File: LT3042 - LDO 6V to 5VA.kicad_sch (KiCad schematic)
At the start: 17 parts, among them IC2 TPS61086DRCR

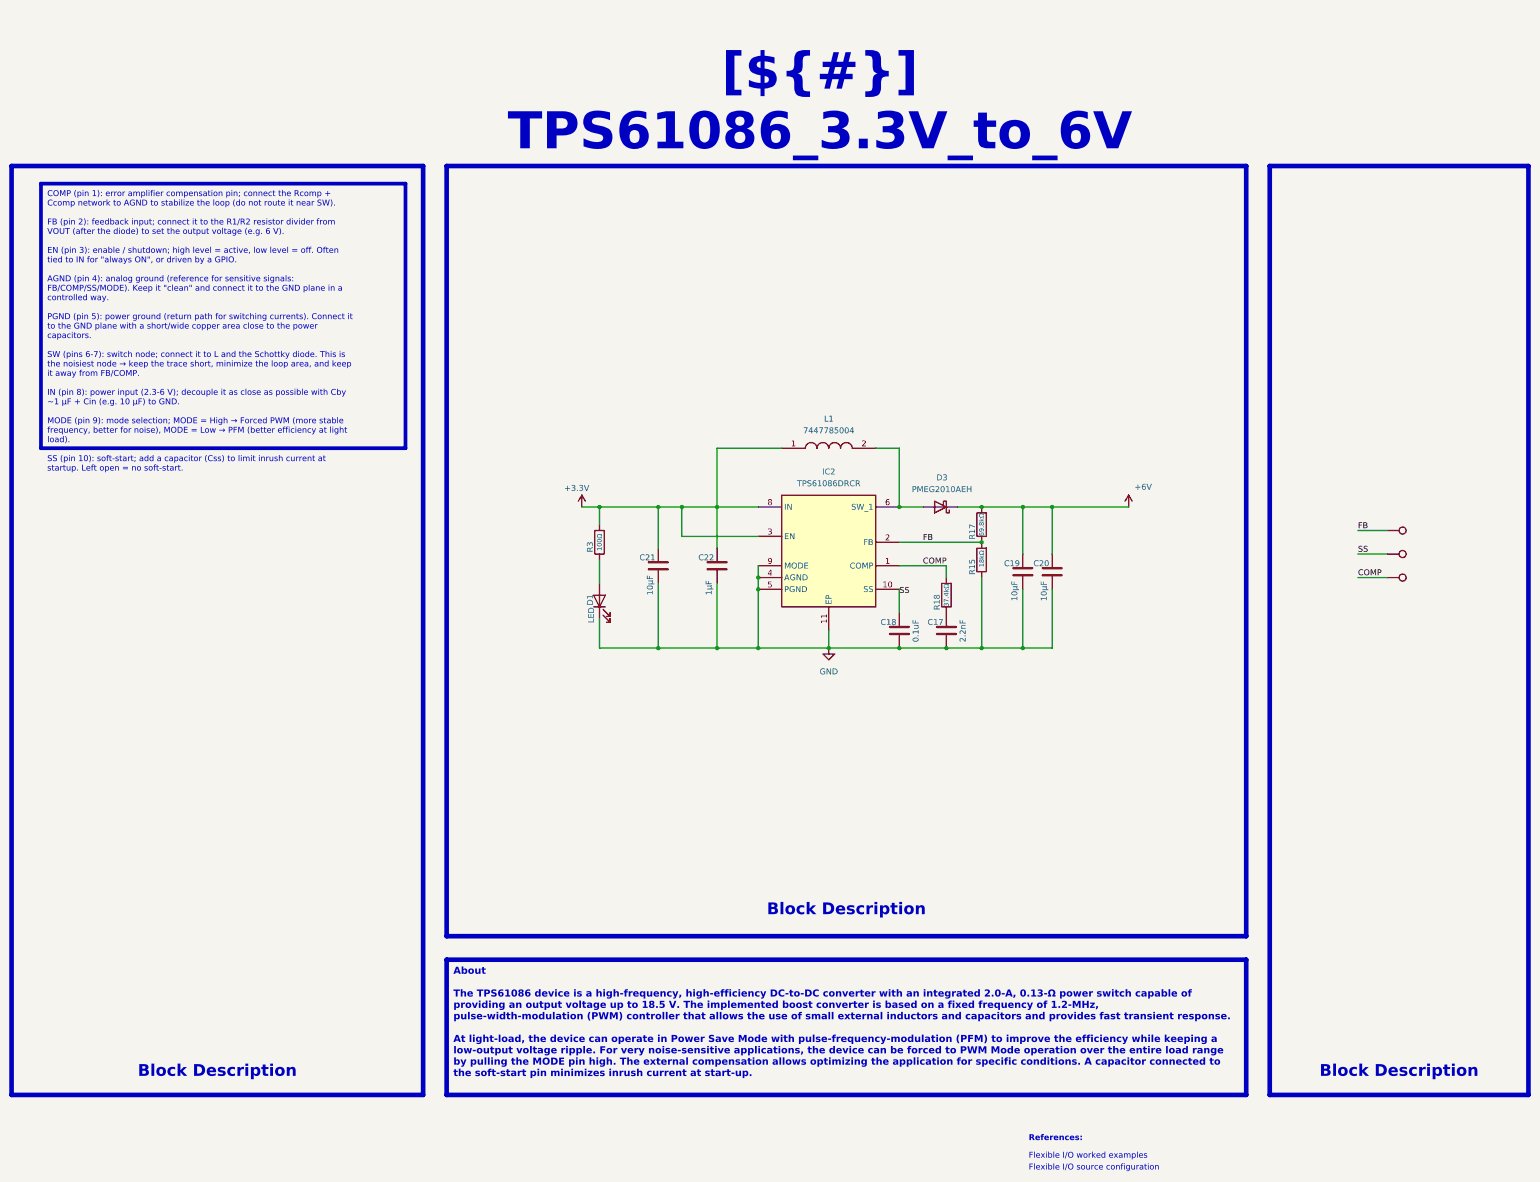
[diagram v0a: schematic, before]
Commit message: Clean up project for KDT template: rename, metadata, KiCad 10 CI
- Rename project Cellule_de_force_V2 -> OPEN_WEIGHT and sheets after their function
  (fix AD7910 -> AD7190 typo), update all sheet/project references in sch/pcb/pro
- Real title-block titles, sheet headers use ${TITLE}, restore KDT drawing sheets,
  remove template leftovers from PCB title block
- kibot_main.yaml: COMPANY = OPEN THRUST LAB, GIT_URL = foukouda/OPEN_WEIGHT
- CI: add KiCad 10 (KiBot v2_dk10), PRELIMINARY variant on dev
- README now generated from kibot_resources/templates/readme.txt; fill CHANGELOG
- Move mechanical CAD to Mechanical/, extend .gitignore, untrack 3Dx logs

Co-Authored-By: Claude Opus 5.5 <noreply@anthropic.com>
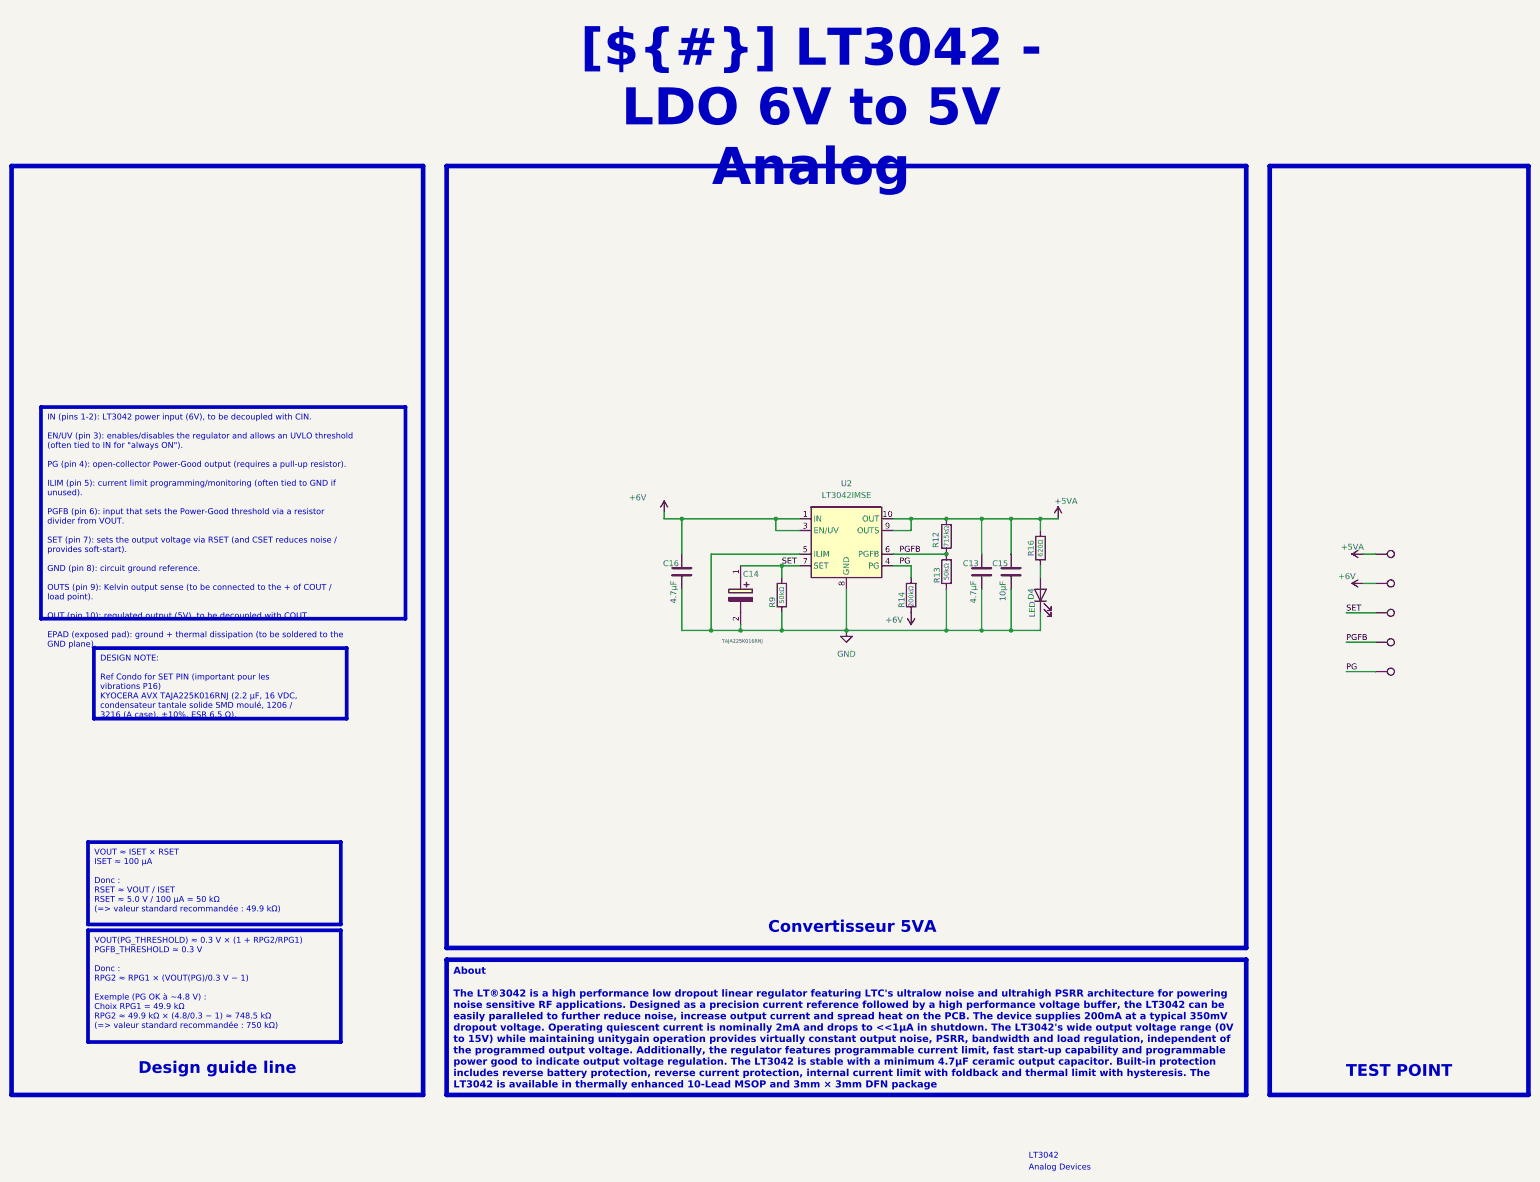
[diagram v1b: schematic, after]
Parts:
- removed C17: 2.2nF, Capacitor_SMD:C_0603_1608Metric, symbol Device:C
- removed C18: 0.1uF, Capacitor_SMD:C_0603_1608Metric, symbol Device:C
- removed C19, C20, C21: 10µF, Capacitor_SMD:C_0603_1608Metric, symbol Device:C
- removed C22: 1µF, Capacitor_SMD:C_0603_1608Metric, symbol Device:C
- removed D1: LED, LED_SMD:LED_0603_1608Metric, symbol Device:LED
- removed D3: PMEG2010AEH, Diode_SMD:D_SOD-123F, symbol Diode:PMEG2010AEH
- removed IC2: TPS61086DRCR, TPS61086DRCR:TPS16412DRCR, symbol TPS61086DRCR:TPS61086DRCR
- removed L1: 7447785004, 7447785004:7447785004, symbol 7447785004:7447785004
- removed R15: 18kΩ, Resistor_SMD:R_0603_1608Metric, symbol Device:R
- removed R17: 69.8kΩ, Resistor_SMD:R_0603_1608Metric, symbol Device:R
- removed R18: 37.4kΩ, Resistor_SMD:R_0603_1608Metric, symbol Device:R
- removed R3: 100Ω, Resistor_SMD:R_0603_1608Metric, symbol Device:R
- removed TP14, TP15, TP16: TestPoint, TestPoint:TestPoint_Pad_D1.5mm, symbol Connector:TestPoint
- added C13, C16: 4.7µF, Capacitor_SMD:C_0603_1608Metric, symbol Device:C
- added C14: TAJA225K016RNJ, CAPPM3216X180N, symbol TAJA225K016RNJ:TAJA225K016RNJ
- added C15: 10µF, Capacitor_SMD:C_0603_1608Metric, symbol Device:C
- added D4: LED, LED_SMD:LED_0603_1608Metric, symbol Device:LED
- added R12: 715kΩ, Resistor_SMD:R_0603_1608Metric, symbol Device:R
- added R13, R9: 50kΩ, Resistor_SMD:R_0603_1608Metric, symbol Device:R
- added R14: 200kΩ, Resistor_SMD:R_0603_1608Metric, symbol Device:R
- added R16: 620Ω, Resistor_SMD:R_0603_1608Metric, symbol Device:R
- added TP10, TP11, TP12, TP13, TP17: TestPoint, TestPoint:TestPoint_Pad_D1.5mm, symbol Connector:TestPoint
- added U2: LT3042IMSE, Package_SO:MSOP-10-1EP_3x3mm_P0.5mm_EP2.2x3.1mm_Mask1.83x1.89mm_ThermalVias, symbol Regulator_Linear:LT3042xMSE
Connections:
- net +6V: now also C16.1, R14.1, TP11.1, U2.1 (IN), U2.2 (IN), U2.3 (EN/UV)
- net GND: now also C13.2, C14.2 (-), C15.2, C16.2, D4.1 (K), R13.1, R9.1, U2.11 (GND), U2.5 (ILIM), U2.8 (GND)
- new net: D4.2 (A), R16.1
- new net +5VA: C13.1, C15.1, R12.2, R16.2, TP10.1, U2.10 (OUT), U2.9 (OUTS)
- new net PG: R14.2, TP17.1, U2.4 (PG)
- new net PGFB: R12.1, R13.2, TP13.1, U2.6 (PGFB)
- new net SET: C14.1 (+), R9.2, TP12.1, U2.7 (SET)
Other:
- note added: "Analog Devices"
- note added: "LT3042"
- note removed: "Flexible I/O source configuration"
- note removed: "Flexible I/O worked examples"
- note removed: "References:"
- title: Sheet Title B -> LT3042 - LDO 6V to 5V Analog

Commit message: Self-contained libraries, JLCPCB rules, ERC/DRC cleanup
- lib/: project symbol library (19 symbols), footprint library (17 footprints)
  and all 3D models (15), referenced through ${KIPRJMOD} + project lib tables.
  A fresh clone now opens with every symbol, footprint and 3D model.
- Remove duplicated / absolute 3D model paths (C:/Users/..., ${KICAD_FOOTPRINT})
- OPEN_WEIGHT.kicad_dru: JLCPCB 4-layer rules; stackup JLC04161H-7628; board minimums
- AD7190 footprint: drop per-pad 0.102 mm mask margin (mask bridges at 0.65 mm pitch)
- Exclude unplaced TP/FID symbols from board; PWR_FLAGs; decorative wires -> lines
- Local text variables in .kicad_pro; Revision History wired to [Unreleased]
- get_changelog.py: accept "## [Unreleased]" without date
ERC: 0 errors. DRC: 0 errors except 10 courtyard overlaps (placement), 0 parity issues.

Co-Authored-By: Claude Opus 5.5 <noreply@anthropic.com>
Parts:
- C13, C15, C16: footprint Capacitor_SMD:C_0603_1608Metric -> OPEN_WEIGHT:C_0603_1608Metric; symbol Device:C -> OPEN_WEIGHT:C
- C14: footprint CAPPM3216X180N -> OPEN_WEIGHT:CAPPM3216X180N; symbol TAJA225K016RNJ:TAJA225K016RNJ -> OPEN_WEIGHT:TAJA225K016RNJ
- D4: footprint LED_SMD:LED_0603_1608Metric -> OPEN_WEIGHT:LED_0603_1608Metric; symbol Device:LED -> OPEN_WEIGHT:LED
- R12, R13, R14, R16, R9: footprint Resistor_SMD:R_0603_1608Metric -> OPEN_WEIGHT:R_0603_1608Metric; symbol Device:R -> OPEN_WEIGHT:R
- TP10: footprint TestPoint:TestPoint_Pad_D1.5mm -> OPEN_WEIGHT:TestPoint_Pad_D1.5mm; symbol Connector:TestPoint -> OPEN_WEIGHT:TestPoint; now left out of the parts list
- TP11, TP12, TP13, TP17: footprint TestPoint:TestPoint_Pad_D1.5mm -> OPEN_WEIGHT:TestPoint_Pad_D1.5mm; symbol Connector:TestPoint -> OPEN_WEIGHT:TestPoint
- U2: footprint Package_SO:MSOP-10-1EP_3x3mm_P0.5mm_EP2.2x3.1mm_Mask1.83x1.89mm_ThermalVias -> OPEN_WEIGHT:MSOP-10-1EP_3x3mm_P0.5mm_EP2.2x3.1mm_Mask1.83x1.89mm_ThermalVias; symbol Regulator_Linear:LT3042xMSE -> OPEN_WEIGHT:LT3042xMSE
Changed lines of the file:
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@@
 	)
 	(symbol
-		(lib_id "Connector:TestPoint")
+		(lib_id "OPEN_WEIGHT:TestPoint")
 		(at 340.36 129.54 270)
 		(unit 1)
@@
 			)
 		)
-		(property "Footprint" "TestPoint:TestPoint_Pad_D1.5mm"
+		(property "Footprint" "OPEN_WEIGHT:TestPoint_Pad_D1.5mm"
 			(at 340.36 134.62 0)
 			(hide yes)
@@
 	)
 	(symbol
-		(lib_id "Regulator_Linear:LT3042xMSE")
+		(lib_id "OPEN_WEIGHT:LT3042xMSE")
 		(at 226.06 118.11 0)
 		(unit 1)
@@
 			)
 		)
-		(property "Footprint" "Package_SO:MSOP-10-1EP_3x3mm_P0.5mm_EP2.2x3.1mm_Mask1.83x1.89mm_ThermalVias"
+		(property "Footprint" "OPEN_WEIGHT:MSOP-10-1EP_3x3mm_P0.5mm_EP2.2x3.1mm_Mask1.83x1.89mm_ThermalVias"
 			(at 226.06 109.855 0)
 			(hide yes)
@@
 	)
 	(symbol
-		(lib_id "Connector:TestPoint")
+		(lib_id "OPEN_WEIGHT:TestPoint")
 		(at 340.36 123.19 270)
 		(unit 1)
 		(body_style 1)
 		(exclude_from_sim no)
-		(in_bom yes)
-		(on_board yes)
-		(in_pos_files yes)
+		(in_bom no)
+		(on_board no)
+		(in_pos_files no)
 		(dnp no)
 		(fields_autoplaced yes)
@@
 			)
 		)
-		(property "Footprint" "TestPoint:TestPoint_Pad_D1.5mm"
+		(property "Footprint" "OPEN_WEIGHT:TestPoint_Pad_D1.5mm"
 			(at 340.36 128.27 0)
 			(hide yes)
@@
 	)
 	(symbol
-		(lib_id "Device:R")
+		(lib_id "OPEN_WEIGHT:R")
 		(at 247.65 119.38 180)
 		(unit 1)
@@
 			)
 		)
-		(property "Footprint" "Resistor_SMD:R_0603_1608Metric"
+		(property "Footprint" "OPEN_WEIGHT:R_0603_1608Metric"
 			(at 249.428 119.38 90)
 			(hide yes)
@@
 	)
 	(symbol
-		(lib_id "Connector:TestPoint")
+		(lib_id "OPEN_WEIGHT:TestPoint")
 		(at 340.36 148.59 270)
 		(unit 1)
@@
 			)
 		)
-		(property "Footprint" "TestPoint:TestPoint_Pad_D1.5mm"
+		(property "Footprint" "OPEN_WEIGHT:TestPoint_Pad_D1.5mm"
 			(at 340.36 153.67 0)
 			(hide yes)
@@
 	)
 	(symbol
-		(lib_id "Device:R")
+		(lib_id "OPEN_WEIGHT:R")
 		(at 240.03 132.08 180)
 		(unit 1)
@@
 			)
 		)
-		(property "Footprint" "Resistor_SMD:R_0603_1608Metric"
+		(property "Footprint" "OPEN_WEIGHT:R_0603_1608Metric"
 			(at 241.808 132.08 90)
 			(hide yes)
@@
 	)
 	(symbol
-		(lib_id "Device:R")
+		(lib_id "OPEN_WEIGHT:R")
 		(at 267.97 121.92 180)
 		(unit 1)
@@
 			)
 		)
-		(property "Footprint" "Resistor_SMD:R_0603_1608Metric"
+		(property "Footprint" "OPEN_WEIGHT:R_0603_1608Metric"
 			(at 269.748 121.92 90)
 			(hide yes)
@@
 	)
 	(symbol
-		(lib_id "Connector:TestPoint")
+		(lib_id "OPEN_WEIGHT:TestPoint")
 		(at 340.36 135.89 270)
 		(unit 1)
@@
 			)
 		)
-		(property "Footprint" "TestPoint:TestPoint_Pad_D1.5mm"
+		(property "Footprint" "OPEN_WEIGHT:TestPoint_Pad_D1.5mm"
 			(at 340.36 140.97 0)
 			(hide yes)
@@
 	)
 	(symbol
-		(lib_id "TAJA225K016RNJ:TAJA225K016RNJ")
+		(lib_id "OPEN_WEIGHT:TAJA225K016RNJ")
 		(at 203.2 125.73 270)
 		(unit 1)
@@
 			)
 		)
-		(property "Footprint" "CAPPM3216X180N"
+		(property "Footprint" "OPEN_WEIGHT:CAPPM3216X180N"
 			(at 107.01 134.62 0)
 			(hide yes)
@@
 	)
 	(symbol
-		(lib_id "Connector:TestPoint")
+		(lib_id "OPEN_WEIGHT:TestPoint")
 		(at 340.36 142.24 270)
 		(unit 1)
@@
 			)
 		)
-		(property "Footprint" "TestPoint:TestPoint_Pad_D1.5mm"
+		(property "Footprint" "OPEN_WEIGHT:TestPoint_Pad_D1.5mm"
 			(at 340.36 147.32 0)
 			(hide yes)
@@
 	)
 	(symbol
-		(lib_id "Device:C")
+		(lib_id "OPEN_WEIGHT:C")
 		(at 261.62 127 0)
 		(unit 1)
@@
 			)
 		)
-		(property "Footprint" "Capacitor_SMD:C_0603_1608Metric"
+		(property "Footprint" "OPEN_WEIGHT:C_0603_1608Metric"
 			(at 262.5852 130.81 0)
 			(hide yes)
@@
 	)
 	(symbol
-		(lib_id "Device:LED")
+		(lib_id "OPEN_WEIGHT:LED")
 		(at 267.97 132.08 90)
 		(unit 1)
@@
 			)
 		)
-		(property "Footprint" "LED_SMD:LED_0603_1608Metric"
+		(property "Footprint" "OPEN_WEIGHT:LED_0603_1608Metric"
 			(at 267.97 132.08 0)
 			(hide yes)
@@
 	)
 	(symbol
-		(lib_id "Device:R")
+		(lib_id "OPEN_WEIGHT:R")
 		(at 212.09 132.08 180)
 		(unit 1)
@@
 			)
 		)
-		(property "Footprint" "Resistor_SMD:R_0603_1608Metric"
+		(property "Footprint" "OPEN_WEIGHT:R_0603_1608Metric"
 			(at 213.868 132.08 90)
 			(hide yes)
@@
 	)
 	(symbol
-		(lib_id "Device:C")
+		(lib_id "OPEN_WEIGHT:C")
 		(at 255.27 127 0)
 		(unit 1)
@@
 			)
 		)
-		(property "Footprint" "Capacitor_SMD:C_0603_1608Metric"
+		(property "Footprint" "OPEN_WEIGHT:C_0603_1608Metric"
 			(at 256.2352 130.81 0)
 			(hide yes)
@@
 	)
 	(symbol
-		(lib_id "Device:C")
+		(lib_id "OPEN_WEIGHT:C")
 		(at 190.5 127 0)
 		(unit 1)
@@
 			)
 		)
-		(property "Footprint" "Capacitor_SMD:C_0603_1608Metric"
+		(property "Footprint" "OPEN_WEIGHT:C_0603_1608Metric"
 			(at 191.4652 130.81 0)
 			(hide yes)
@@
 	)
 	(symbol
-		(lib_id "Device:R")
+		(lib_id "OPEN_WEIGHT:R")
 		(at 247.65 127 180)
 		(unit 1)
@@
 			)
 		)
-		(property "Footprint" "Resistor_SMD:R_0603_1608Metric"
+		(property "Footprint" "OPEN_WEIGHT:R_0603_1608Metric"
 			(at 249.428 127 90)
 			(hide yes)
